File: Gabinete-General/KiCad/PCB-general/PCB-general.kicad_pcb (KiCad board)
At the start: 2 copper layers, 50 x 100 mm, 18 parts, among them J1 Conn_01x02, J2 Conn_01x02, J3 TFT Display, J4 PCIe X4, SW1 RotaryEncoder_Switch, U1 ESP32-S3-DevKitC, U2 LM7805_TO220

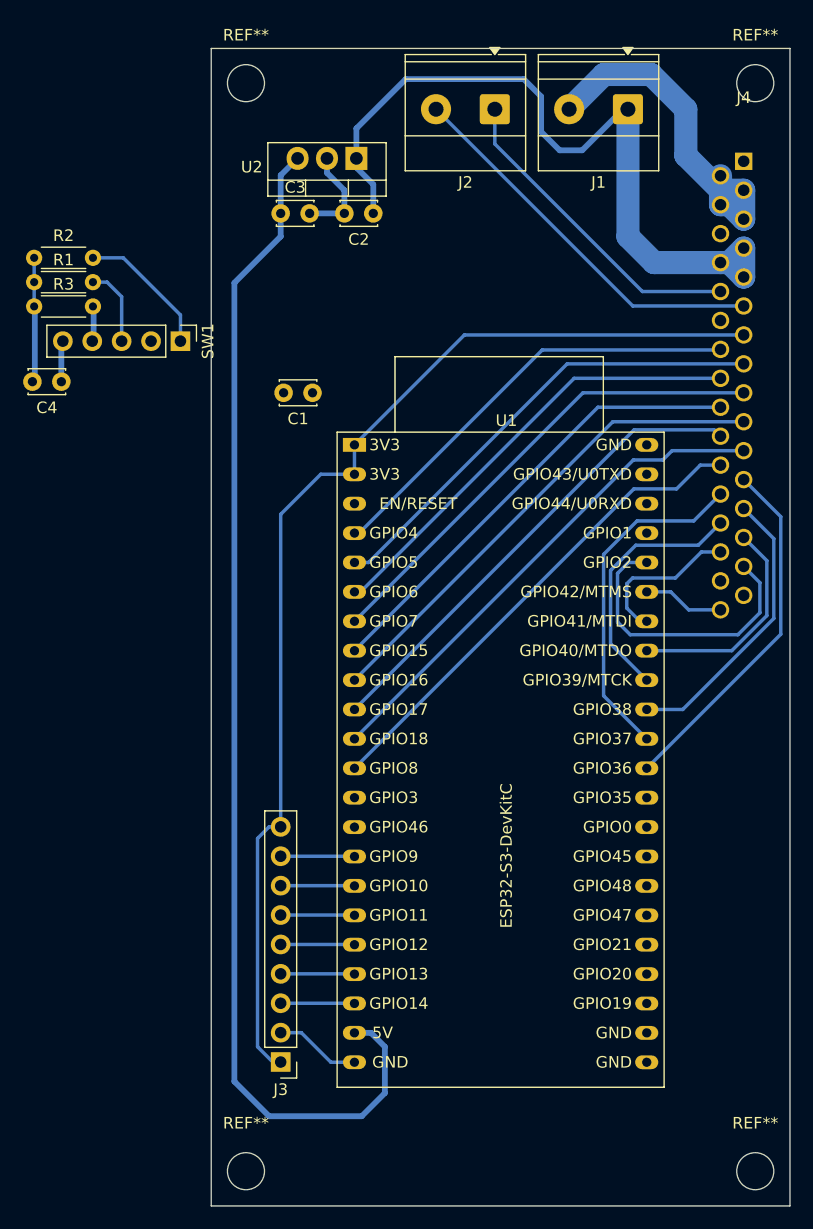
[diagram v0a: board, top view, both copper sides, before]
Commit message: Finalizar diseño PCB apta para planchado
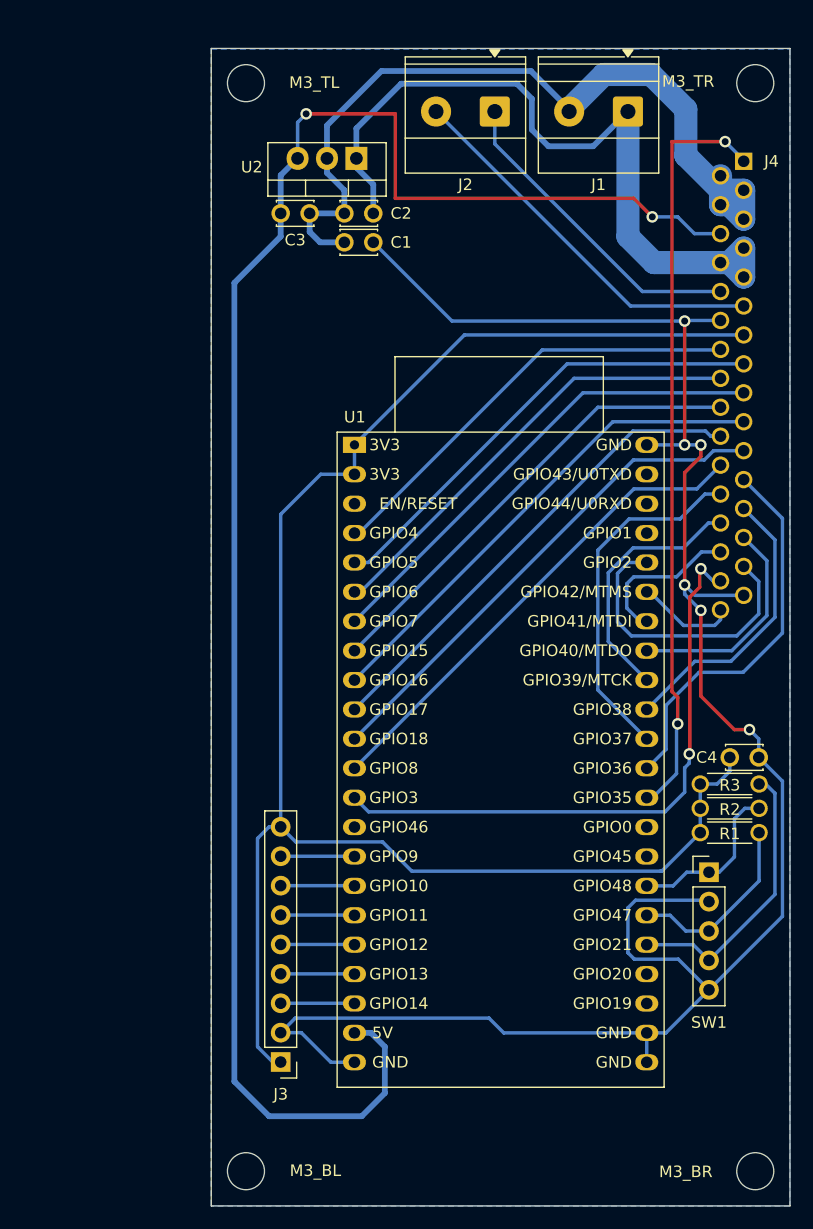
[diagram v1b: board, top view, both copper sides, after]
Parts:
- moved R1 74.7 mm to (197.2, 113.5)
- moved R2 74.7 mm to (197.2, 111.4)
- moved R3 70.8 mm to (197.2, 109.3)
- moved C4 68.4 mm to (202.3, 107.0)
- moved SW1 64.7 mm to (198.0, 116.9), turned to 0 degrees
- moved C1 13.3 mm to (166.5, 62.5), turned to 0 degrees
- moved J1 0.20 mm to (191.0, 51.2)
- moved J2 0.20 mm to (179.5, 51.2)
- renumbered REF** to M3_BL, REF** to M3_BR, REF** to M3_TL, REF** to M3_TR
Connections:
- SW1 pad 1: (no net) -> ROTARY_CLK
- SW1 pad 2: (no net) -> AGND
- SW1 pad 3: (no net) -> ROTARY_DATA
- SW1 pad 4: (no net) -> ROTARY_SW
- SW1 pad 5: (no net) -> AGND
- U1 pad 28: ROTARY_CLK -> ROTARY_DATA
- U1 pad 29: ROTARY_DATA -> ROTARY_CLK
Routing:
- net AGND: track 11.0 -> 177.6 mm, vias 0 -> 6
- net PCIe_HP_Power: track 0.00 -> 65.8 mm, vias 0 -> 2
- net PCIe_MODULE_IDENT: track 0.00 -> 51.7 mm, vias 0 -> 2
- net 5Vdc: track 104.2 -> 152.7 mm, vias 0 -> 2
- net 3.3Vdc: track 108.7 -> 145.5 mm
- net PGND: track 38.5 -> 70.7 mm
- net ROTARY_SW: track 3.05 -> 24.4 mm
- net ROTARY_DATA: track 6.90 -> 16.2 mm
- net ROTARY_CLK: track 11.9 -> 14.4 mm
- net PCIe_S10: track 31.1 -> 33.4 mm
- net PCIe_HP_Signal: track 7.02 -> 8.63 mm
- net PCIe_S11: track 29.7 -> 30.7 mm
- net 12Vdc: track 65.7 -> 65.0 mm
- added copper zone on B.Cu, net AGND
